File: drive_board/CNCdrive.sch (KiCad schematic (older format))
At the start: 3 parts, among them U1 DRV8711

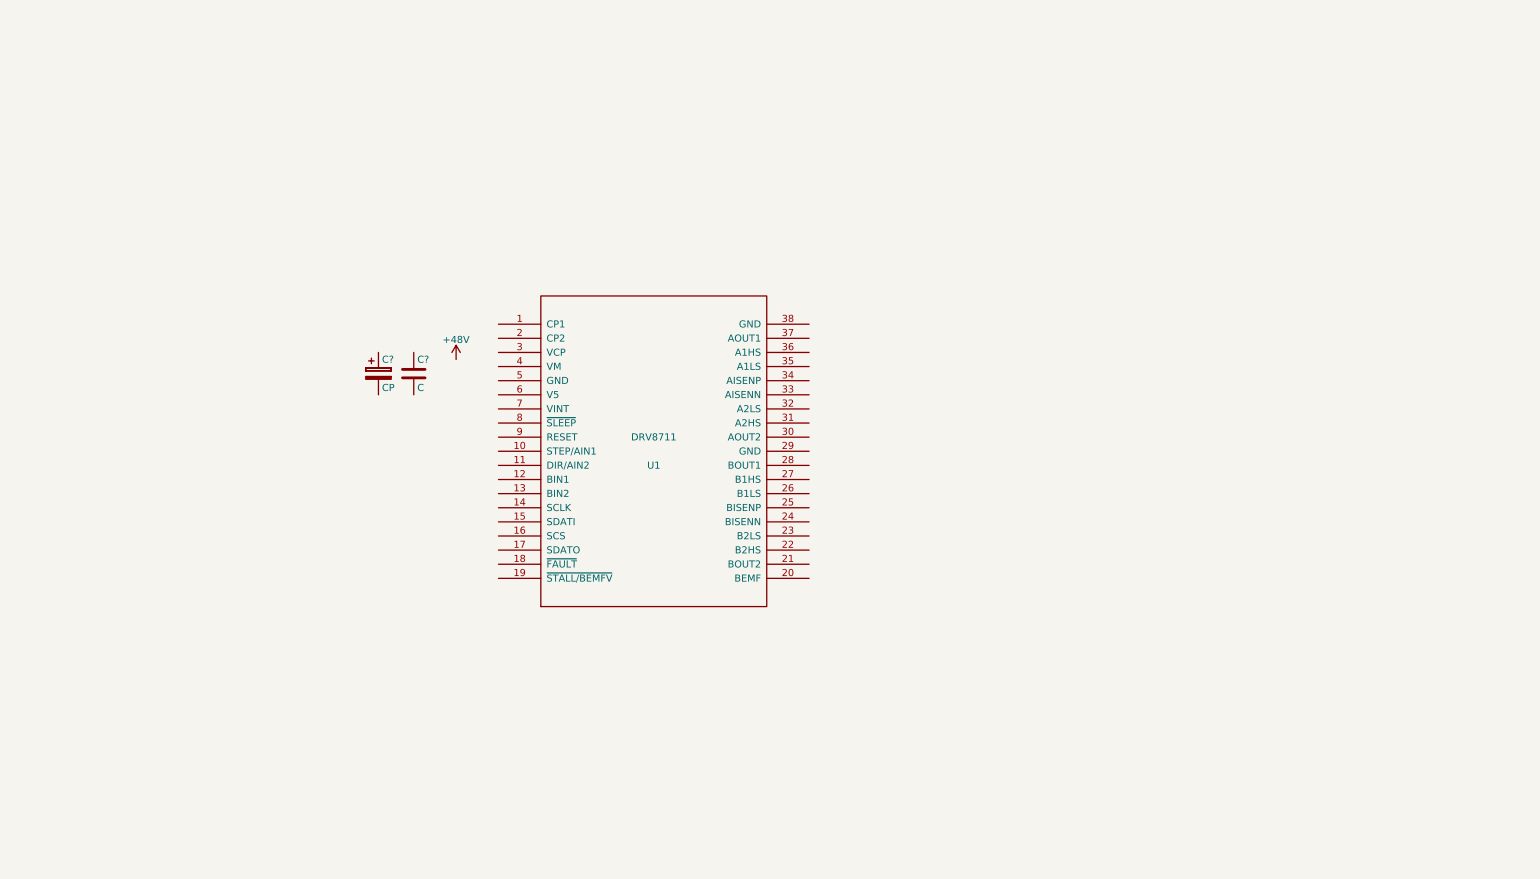
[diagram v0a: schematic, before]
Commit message: added most parts
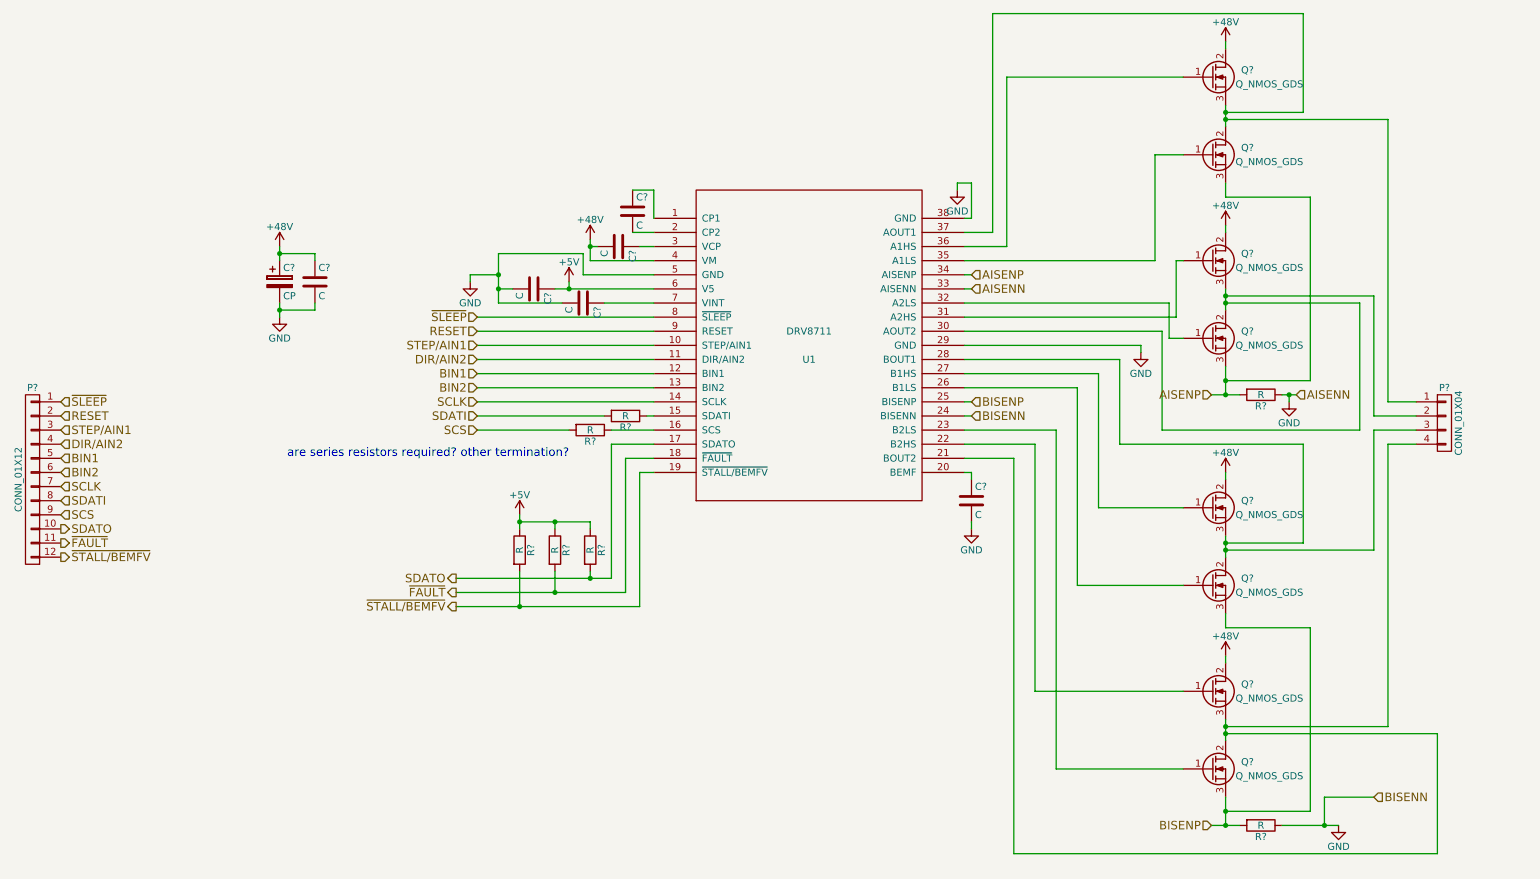
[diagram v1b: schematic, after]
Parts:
- added C? (x5): C, symbol C
- added P?: CONN_01X04, symbol CONN_01X04
- added P?: CONN_01X12, symbol CONN_01X12
- added Q? (x8): Q_NMOS_GDS, symbol Q_NMOS_GDS
- added R? (x7): R, symbol R
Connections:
- net +48V: now also C?.1, U1.4 (VM), C?.1, C?.2, Q?.2 (D), Q?.2 (D), Q?.2 (D), Q?.2 (D)
- net at U1.1 (CP1): now also C?.1
- net STEP/AIN1: now reaches U1.10 (STEP/AIN1)
- net STEP/AIN1: now also P?.3 (P3)
- net DIR/AIN2: now reaches U1.11 (DIR/AIN2)
- net DIR/AIN2: now also P?.4 (P4)
- net BIN1: now reaches U1.12 (BIN1)
- net BIN1: now also P?.5 (P5)
- net BIN2: now reaches U1.13 (BIN2)
- net BIN2: now also P?.6 (P6)
- net SCLK: now reaches U1.14 (SCLK)
- net SCLK: now also P?.7 (P7)
- net at U1.15 (SDATI): now also R?.1
- net at U1.16 (SCS): now also R?.1
- net SDATO: now reaches U1.17 (SDATO)
- net SDATO: now also P?.10 (P10), R?.2
- net ~FAULT: now reaches U1.18 (~FAULT)
- net ~FAULT: now also P?.11 (P11), R?.2
- net ~STALL/BEMFV: now reaches U1.19 (~STALL/BEMFV)
- net ~STALL/BEMFV: now also P?.12 (P12), R?.2
- net at U1.2 (CP2): now also C?.2
- net at U1.20 (BEMF): now also C?.1
- net at U1.21 (BOUT2): now also P?.4 (P4), Q?.2 (D), Q?.3 (S)
- net at U1.22 (B2HS): now also Q?.1 (G)
- net at U1.23 (B2LS): now also Q?.1 (G)
- net GND: now reaches U1.24 (BISENN)
- net GND: now also C?.2, U1.29 (GND), U1.33 (AISENN), U1.38 (GND), U1.5 (GND), C?.2, C?.2, C?.2, C?.2, R?.1, R?.1
- net BISENP: now reaches U1.25 (BISENP)
- net BISENP: now also Q?.3 (S), Q?.3 (S), R?.2
- net at U1.26 (B1LS): now also Q?.1 (G)
- net at U1.27 (B1HS): now also Q?.1 (G)
- net at U1.28 (BOUT1): now also P?.3 (P3), Q?.2 (D), Q?.3 (S)
- net at U1.3 (VCP): now also C?.1
- net at U1.30 (AOUT2): now also P?.2 (P2), Q?.2 (D), Q?.3 (S)
- net at U1.31 (A2HS): now also Q?.1 (G)
- net at U1.32 (A2LS): now also Q?.1 (G)
- net AISENP: now reaches U1.34 (AISENP)
- net AISENP: now also Q?.3 (S), Q?.3 (S), R?.2
- net at U1.35 (A1LS): now also Q?.1 (G)
- net at U1.36 (A1HS): now also Q?.1 (G)
- net at U1.37 (AOUT1): now also P?.1 (P1), Q?.2 (D), Q?.3 (S)
- net +5V: now reaches U1.6 (V5)
- net +5V: now also C?.1, R?.1, R?.1, R?.1
- net at U1.7 (VINT): now also C?.1
- net ~SLEEP: now reaches U1.8 (~SLEEP)
- net ~SLEEP: now also P?.1 (P1)
- net RESET: now reaches U1.9 (RESET)
- net RESET: now also P?.2 (P2)
- new net SCS: P?.9 (P9), R?.2
- new net SDATI: P?.8 (P8), R?.2
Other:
- note added: "are series resistors required? other termination?"
- moved on the sheet: C?, U1

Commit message: main parts added, most values are correct
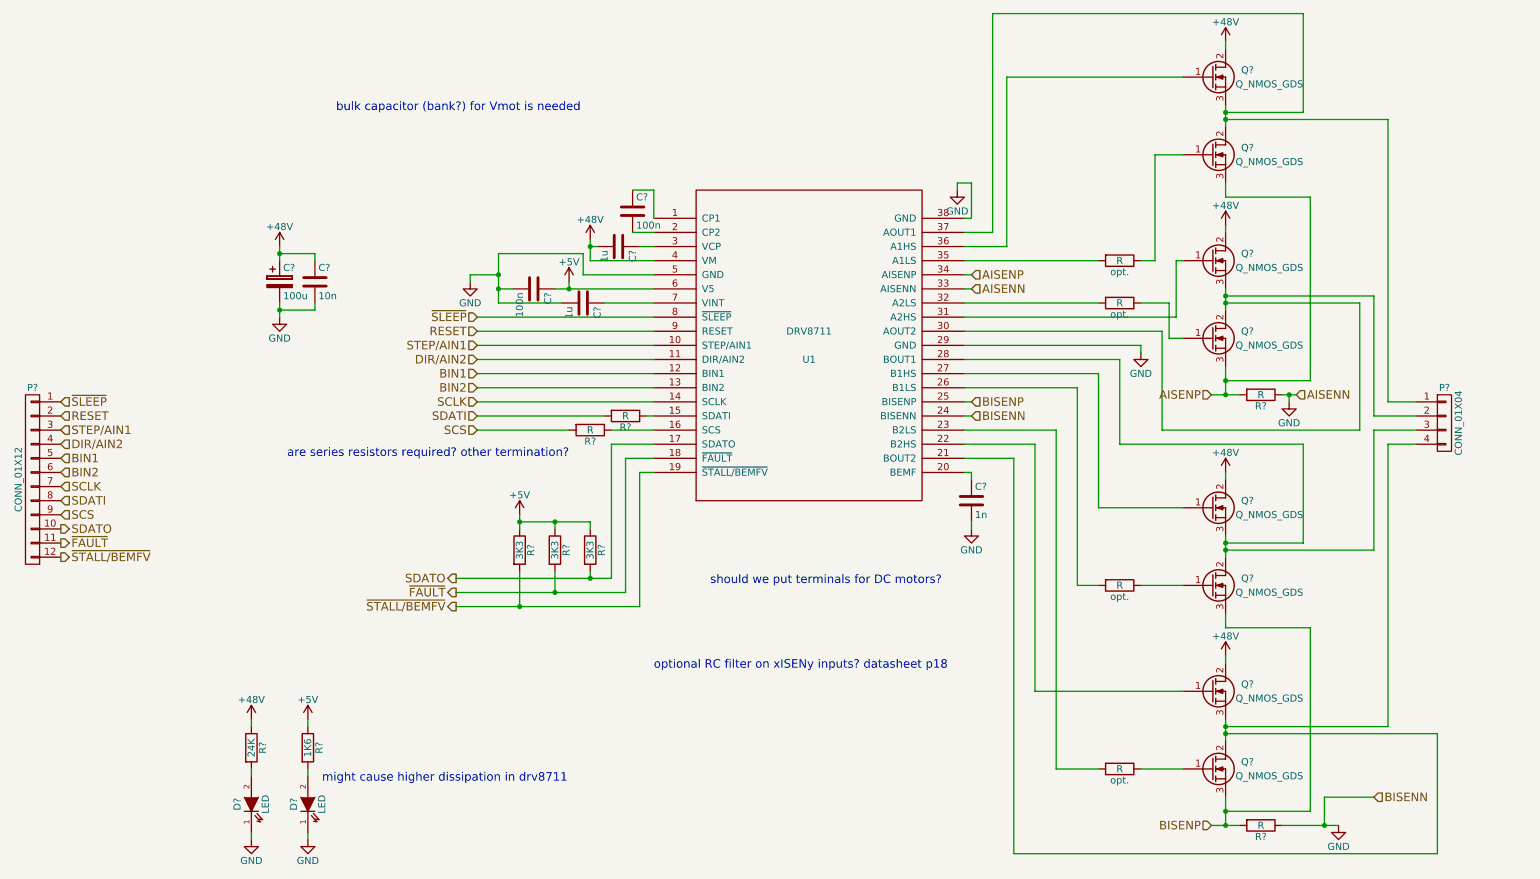
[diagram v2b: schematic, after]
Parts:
- added D? (x2): LED, symbol LED
- added R?: 24K, symbol R
- added R?: 1K6, symbol R
- added opt. (x4): R, symbol R
- C? (x2): value C -> 100n
- C?: value CP -> 100u
- C?: value C -> 10n
- C? (x2): value C -> 1u
- C?: value C -> 1n
- R? (x3): value R -> 3K3
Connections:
- net +48V: now also R?.1
- net +5V: now also R?.1
- net GND: now also D?.1 (K), D?.1 (K)
- net at U1.23 (B2LS): now also opt..2; no longer Q?.1 (G)
- net at U1.26 (B1LS): now also opt..2; no longer Q?.1 (G)
- net at U1.32 (A2LS): now also opt..2; no longer Q?.1 (G)
- net at U1.35 (A1LS): now also opt..2; no longer Q?.1 (G)
- new net: Q?.1 (G), opt..1 (x4)
- new net: D?.2 (A), R?.2 (x2)
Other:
- note added: "bulk capacitor (bank?) for Vmot is needed"
- note added: "might cause higher dissipation in drv8711\n"
- note added: "optional RC filter on xISENy inputs? datasheet p18"
- note added: "should we put terminals for DC motors?"
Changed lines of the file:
@@
 P 5100 1950
 F 0 "C?" H 5125 2050 50  0000 L CNN
-F 1 "C" H 5125 1850 50  0000 L CNN
+F 1 "100n" H 5125 1850 50  0000 L CNN
 F 2 "" H 5138 1800 50  0000 C CNN
 F 3 "" H 5100 1950 50  0000 C CNN
@@
 P 2600 2450
 F 0 "C?" H 2625 2550 50  0000 L CNN
-F 1 "CP" H 2625 2350 50  0000 L CNN
+F 1 "100u" H 2625 2350 50  0000 L CNN
 F 2 "" H 2638 2300 50  0000 C CNN
 F 3 "" H 2600 2450 50  0000 C CNN
@@
 P 4800 4350
 F 0 "R?" V 4880 4350 50  0000 C CNN
-F 1 "R" V 4800 4350 50  0000 C CNN
+F 1 "3K3" V 4800 4350 50  0000 C CNN
 F 2 "" V 4730 4350 50  0000 C CNN
 F 3 "" H 4800 4350 50  0000 C CNN
@@
 P 2850 2450
 F 0 "C?" H 2875 2550 50  0000 L CNN
-F 1 "C" H 2875 2350 50  0000 L CNN
+F 1 "10n" H 2875 2350 50  0000 L CNN
 F 2 "" H 2888 2300 50  0000 C CNN
 F 3 "" H 2850 2450 50  0000 C CNN
@@
 P 5000 2200
 F 0 "C?" H 5025 2300 50  0000 L CNN
-F 1 "C" H 5025 2100 50  0000 L CNN
+F 1 "1u" H 5025 2100 50  0000 L CNN
 F 2 "" H 5038 2050 50  0000 C CNN
 F 3 "" H 5000 2200 50  0000 C CNN
@@
 P 4750 2600
 F 0 "C?" H 4775 2700 50  0000 L CNN
-F 1 "C" H 4775 2500 50  0000 L CNN
+F 1 "1u" H 4775 2500 50  0000 L CNN
 F 2 "" H 4788 2450 50  0000 C CNN
 F 3 "" H 4750 2600 50  0000 C CNN
@@
 P 4400 2500
 F 0 "C?" H 4425 2600 50  0000 L CNN
-F 1 "C" H 4425 2400 50  0000 L CNN
+F 1 "100n" H 4425 2400 50  0000 L CNN
 F 2 "" H 4438 2350 50  0000 C CNN
 F 3 "" H 4400 2500 50  0000 C CNN
@@
 P 4550 4350
 F 0 "R?" V 4630 4350 50  0000 C CNN
-F 1 "R" V 4550 4350 50  0000 C CNN
+F 1 "3K3" V 4550 4350 50  0000 C CNN
 F 2 "" V 4480 4350 50  0000 C CNN
 F 3 "" H 4550 4350 50  0000 C CNN
@@
 P 4300 4350
 F 0 "R?" V 4380 4350 50  0000 C CNN
-F 1 "R" V 4300 4350 50  0000 C CNN
+F 1 "3K3" V 4300 4350 50  0000 C CNN
 F 2 "" V 4230 4350 50  0000 C CNN
 F 3 "" H 4300 4350 50  0000 C CNN
@@
 P 7500 4000
 F 0 "C?" H 7525 4100 50  0000 L CNN
-F 1 "C" H 7525 3900 50  0000 L CNN
+F 1 "1n" H 7525 3900 50  0000 L CNN
 F 2 "" H 7538 3850 50  0000 C CNN
 F 3 "" H 7500 4000 50  0000 C CNN
@@
 	7750 1000 9000 1000
 Wire Wire Line
-	7450 2300 8800 2300
-Wire Wire Line
 	8800 2300 8800 1550
 Wire Wire Line
@@
 	7650 2100 7450 2100
 Connection ~ 9300 1250
-Wire Wire Line
-	7450 2600 8900 2600
 Wire Wire Line
 	8900 2600 8900 2850
@@
 Wire Wire Line
 	10000 6100 10350 6100
-Wire Wire Line
-	8250 4600 9000 4600
 Connection ~ 9300 4300
-Wire Wire Line
-	8100 5900 9000 5900
 Wire Wire Line
 	7950 5350 9000 5350
@@
 Text HLabel 1050 3300 2    60   Input ~ 0
 ~SLEEP
+$Comp
+L R opt.
+U 1 1 56D1F618
+P 8550 2300
+F 0 "opt." V 8630 2300 50  0000 C CNN
+F 1 "R" V 8550 2300 50  0000 C CNN
+F 2 "" V 8480 2300 50  0000 C CNN
+F 3 "" H 8550 2300 50  0000 C CNN
+	1    8550 2300
+	0    1    1    0
+$EndComp
+$Comp
+L R opt.
+U 1 1 56D1FE78
+P 8550 2600
+F 0 "opt." V 8630 2600 50  0000 C CNN
+F 1 "R" V 8550 2600 50  0000 C CNN
+F 2 "" V 8480 2600 50  0000 C CNN
+F 3 "" H 8550 2600 50  0000 C CNN
+	1    8550 2600
+	0    1    1    0
+$EndComp
+$Comp
+L R opt.
+U 1 1 56D1FF00
+P 8550 4600
+F 0 "opt." V 8630 4600 50  0000 C CNN
+F 1 "R" V 8550 4600 50  0000 C CNN
+F 2 "" V 8480 4600 50  0000 C CNN
+F 3 "" H 8550 4600 50  0000 C CNN
+	1    8550 4600
+	0    1    1    0
+$EndComp
+$Comp
+L R opt.
+U 1 1 56D20E54
+P 8550 5900
+F 0 "opt." V 8630 5900 50  0000 C CNN
+F 1 "R" V 8550 5900 50  0000 C CNN
+F 2 "" V 8480 5900 50  0000 C CNN
+F 3 "" H 8550 5900 50  0000 C CNN
+	1    8550 5900
+	0    1    1    0
+$EndComp
+Wire Wire Line
+	8800 2300 8700 2300
+Wire Wire Line
+	8900 2600 8700 2600
+Wire Wire Line
+	8400 2300 7450 2300
+Wire Wire Line
+	8400 2600 7450 2600
+Wire Wire Line
+	9000 4600 8700 4600
+Wire Wire Line
+	8250 4600 8400 4600
+Wire Wire Line
+	9000 5900 8700 5900
+Wire Wire Line
+	8100 5900 8400 5900
+$Comp
+L +48V #PWR?
+U 1 1 56D29B9F
+P 2400 5550
+F 0 "#PWR?" H 2400 5400 50  0001 C CNN
+F 1 "+48V" H 2400 5690 50  0000 C CNN
+F 2 "" H 2400 5550 50  0000 C CNN
+F 3 "" H 2400 5550 50  0000 C CNN
+	1    2400 5550
+	1    0    0    -1
+$EndComp
+$Comp
+L +5V #PWR?
+U 1 1 56D2A11A
+P 2800 5550
+F 0 "#PWR?" H 2800 5400 50  0001 C CNN
+F 1 "+5V" H 2800 5690 50  0000 C CNN
+F 2 "" H 2800 5550 50  0000 C CNN
+F 3 "" H 2800 5550 50  0000 C CNN
+	1    2800 5550
+	1    0    0    -1
+$EndComp
+$Comp
+L R R?
+U 1 1 56D2C0CA
+P 2400 5750
+F 0 "R?" V 2480 5750 50  0000 C CNN
+F 1 "24K" V 2400 5750 50  0000 C CNN
+F 2 "" V 2330 5750 50  0000 C CNN
+F 3 "" H 2400 5750 50  0000 C CNN
+	1    2400 5750
+	1    0    0    -1
+$EndComp
+$Comp
+L R R?
+U 1 1 56D2CE52
+P 2800 5750
+F 0 "R?" V 2880 5750 50  0000 C CNN
+F 1 "1K6" V 2800 5750 50  0000 C CNN
+F 2 "" V 2730 5750 50  0000 C CNN
+F 3 "" H 2800 5750 50  0000 C CNN
+	1    2800 5750
+	1    0    0    -1
+$EndComp
+$Comp
+L LED D?
+U 1 1 56D2D02E
+P 2400 6150
+F 0 "D?" H 2400 6250 50  0000 C CNN
+F 1 "LED" H 2400 6050 50  0000 C CNN
+F 2 "" H 2400 6150 50  0000 C CNN
+F 3 "" H 2400 6150 50  0000 C CNN
+	1    2400 6150
+	0    -1   -1   0
+$EndComp
+$Comp
+L LED D?
+U 1 1 56D2D2CB
+P 2800 6150
+F 0 "D?" H 2800 6250 50  0000 C CNN
+F 1 "LED" H 2800 6050 50  0000 C CNN
+F 2 "" H 2800 6150 50  0000 C CNN
+F 3 "" H 2800 6150 50  0000 C CNN
+	1    2800 6150
+	0    -1   -1   0
+$EndComp
+$Comp
+L GND #PWR?
+U 1 1 56D2DDF9
+P 2400 6400
+F 0 "#PWR?" H 2400 6150 50  0001 C CNN
+F 1 "GND" H 2400 6250 50  0000 C CNN
+F 2 "" H 2400 6400 50  0000 C CNN
+F 3 "" H 2400 6400 50  0000 C CNN
+	1    2400 6400
+	1    0    0    -1
+$EndComp
+$Comp
+L GND #PWR?
+U 1 1 56D2E266
+P 2800 6400
+F 0 "#PWR?" H 2800 6150 50  0001 C CNN
+F 1 "GND" H 2800 6250 50  0000 C CNN
+F 2 "" H 2800 6400 50  0000 C CNN
+F 3 "" H 2800 6400 50  0000 C CNN
+	1    2800 6400
+	1    0    0    -1
+$EndComp
+Wire Wire Line
+	2400 5550 2400 5600
+Wire Wire Line
+	2800 5550 2800 5600
+Wire Wire Line
+	2400 5900 2400 5950
+Wire Wire Line
+	2800 5900 2800 5950
+Wire Wire Line
+	2400 6350 2400 6400
+Wire Wire Line
+	2800 6350 2800 6400
+Text Notes 2900 6000 0    60   ~ 0
+might cause higher dissipation in drv8711\n
+Text Notes 5650 4600 0    60   ~ 0
+should we put terminals for DC motors?
+Text Notes 5250 5200 0    60   ~ 0
+optional RC filter on xISENy inputs? datasheet p18
+Text Notes 3000 1250 0    60   ~ 0
+bulk capacitor (bank?) for Vmot is needed
 $EndSCHEMATC

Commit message: Almost finshed, fully commented
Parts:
- removed P?: CONN_01X12, symbol CONN_01X12
- removed R? (x2): R, symbol R
- added C7: 1000u, symbol CP
- added D10, D3, D4, D5, D6, D7, D8, D9: ZENER opt., symbol ZENER
- added P1: CONN_01X14, symbol CONN_01X14
- gave numbers to parts that had none: 25
- renumbered opt. to opt.1, opt. to opt.2, opt. to opt.3, opt. to opt.4
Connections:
- net +48V: now also C7.1
- net AISENP: now also D4.2 (A), D6.2 (A)
- net BIN1: now also P1.5 (P5)
- net BIN2: now also P1.6 (P6)
- net BISENP: now also D10.2 (A), D8.2 (A)
- net DIR/AIN2: now also P1.4 (P4)
- net GND: now also C7.2, P1.14 (P14)
- net RESET: now also P1.2 (P2)
- net SCLK: now also P1.7 (P7)
- net SCS: now also U1.16 (SCS), P1.9 (P9)
- net SDATI: now also U1.15 (SDATI), P1.8 (P8)
- net SDATO: now also P1.10 (P10)
- net STEP/AIN1: now also P1.3 (P3)
- net ~FAULT: now also P1.11 (P11)
- net ~SLEEP: now also P1.1 (P1)
- net ~STALL/BEMFV: now also P1.12 (P12)
- net at P2.4 (P4), Q7.3 (S), Q8.2 (D)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: now also D9.2 (A)
- net at Q7.1 (G), U1.22 (B2HS): now also D9.1 (K)
- net at Q5.1 (G), U1.27 (B1HS): now also D7.1 (K)
- net at P2.3 (P3), Q5.3 (S), Q6.2 (D)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: now also D7.2 (A)
- net at P2.2 (P2), Q3.3 (S), Q4.2 (D)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: now also D5.2 (A)
- net at Q3.1 (G), U1.31 (A2HS): now also D5.1 (K)
- net at Q1.1 (G), U1.36 (A1HS): now also D3.1 (K)
- net at P2.1 (P1), Q1.3 (S), Q2.2 (D)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: now also D3.2 (A)
- net at Q2.1 (G), opt.1.1: now also D4.1 (K)
- net at Q4.1 (G), opt.2.1: now also D6.1 (K)
- net at Q6.1 (G), opt.3.1: now also D8.1 (K)
- net at Q8.1 (G), opt.4.1: now also D10.1 (K)
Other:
- note added: "+protection diodes to G-S?\n"
- moved on the sheet: C3, C4, Q2, Q4, Q6, Q8, R3, R4, R5, R7, opt.3, opt.4
